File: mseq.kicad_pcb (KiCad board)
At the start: 2 copper layers, 100 x 65 mm, 66 parts, among them J1 Screen_I2C, J2 TC2030-NL, P1 USB_C_Plug_USB2.0, SW1 RESET, SW2 ON/OFF, SW3 MS/SLAVE, SW4 BOOT, U1 SN74AHCT125DR, U2 H11L1M, U3 MCP1703Ax-330xxTT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

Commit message: V0.1.0 done
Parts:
- moved MIDI_IN1 2.60 mm to (61.6, 55.9)
- moved MIDI_OUT1 2.60 mm to (88.8, 55.9)
- moved MIDI_THRU1 2.55 mm to (116.3, 55.9)
- moved P1 0.66 mm to (142.3, 52.5)
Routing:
- net Net-(FB2-Pad2): track 4.05 -> 6.69 mm
- net GND: track 554.9 -> 552.3 mm
- net Net-(FB7-Pad2): track 3.61 -> 6.21 mm
- net Net-(FB4-Pad1): track 3.32 -> 5.92 mm
- net Net-(FB1-Pad2): track 3.72 -> 6.32 mm
- net Net-(FB3-Pad1): track 3.87 -> 6.40 mm
- net Net-(FB5-Pad2): track 4.56 -> 6.54 mm
- net Net-(SW2-B): track 23.4 -> 22.2 mm
- net unconnected-(MIDI_IN1-GND-PadG1): track 21.1 -> 22.1 mm
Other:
- board size 100 x 65 mm -> 100 x 67 mm

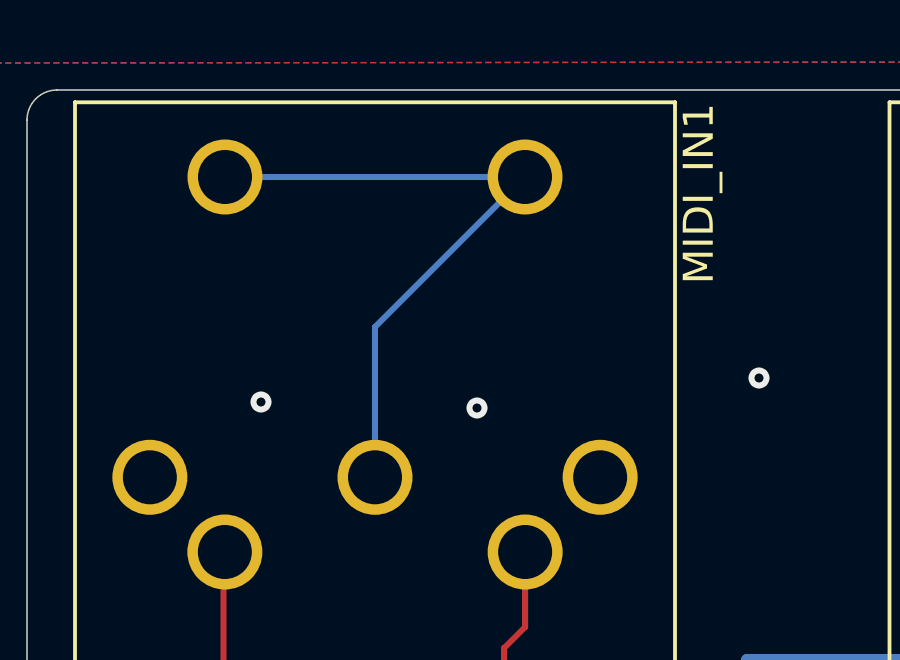
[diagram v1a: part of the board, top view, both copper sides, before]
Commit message: USB bug fixed and new JTAG connector
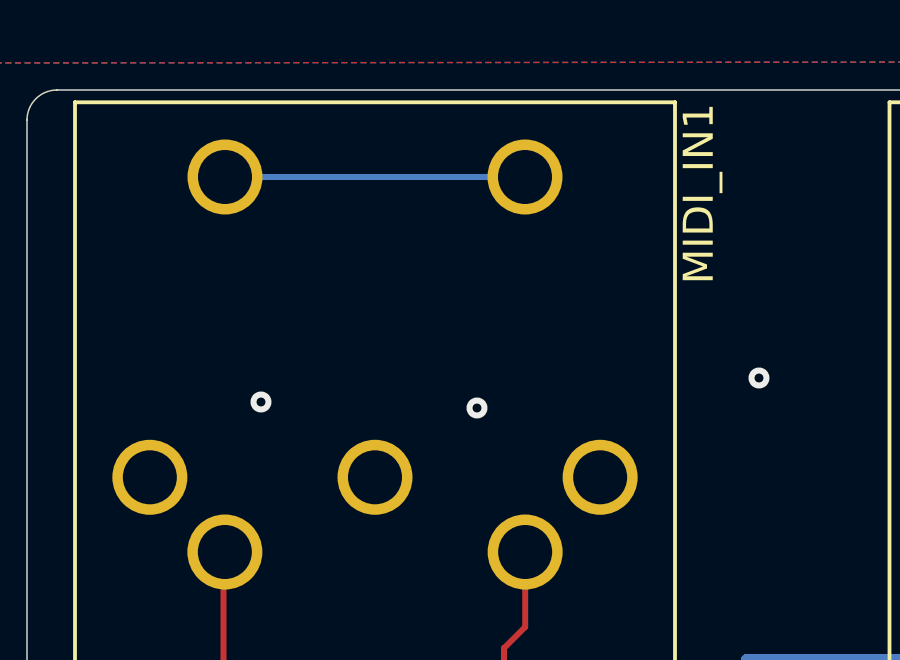
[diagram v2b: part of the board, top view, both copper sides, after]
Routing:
- net unconnected-(MIDI_IN1-GND-PadG1): track 22.1 -> 10.00 mm
